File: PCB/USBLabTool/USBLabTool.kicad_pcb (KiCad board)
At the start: 2 copper layers, 9.1 x 5.9 mm, 209 parts, among them J1 Chanel 1 input, J10 T_pwm, J11 T_buf, J12 T_buf, J13 ADC2, J14 ADC1, J15 +3.3VA, J16 +3.3VA, J17 2x01, J18 02x02, J19 T_N5V, J2 Chanel 0 input, J20 USB_C_Receptacle, J3 T_att, J4 T_att, J5 T_acdc, J6 T_acdc, J7 T_amp, J8 T_amp, J9 T_pwm, K1 G5V-2, K2 G5V-2, SW2 PTH_RA_h7.5mm, U1 AQY284SX, U10 Opamp_Quad, U11 DG403, U12 STM32H562VGTx, U13 r1283, U14 XC6206PxxxMR, U15 XC6206PxxxMR, U16 LTC1983ES6-5#TRPBF, U17 TCPP01-M12, U2 AQY284SX, U3 CD74HC4316M96, U4 LMP7718, U5 CD74HC4316M96, U6 LMP7718, U7 OPA863, U8 OPA863, U9 Opamp_Quad, Y1 32.768kHz

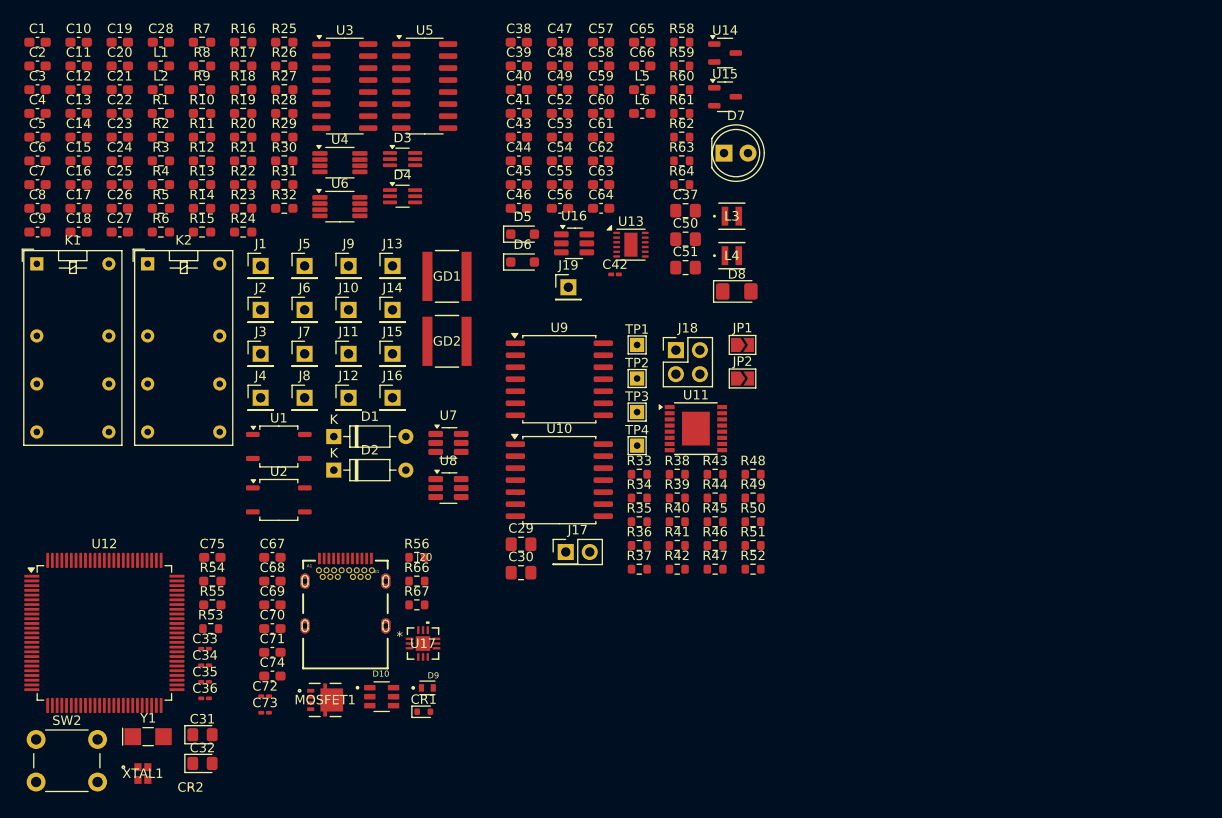
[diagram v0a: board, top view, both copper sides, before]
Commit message: footprint with minor fixes
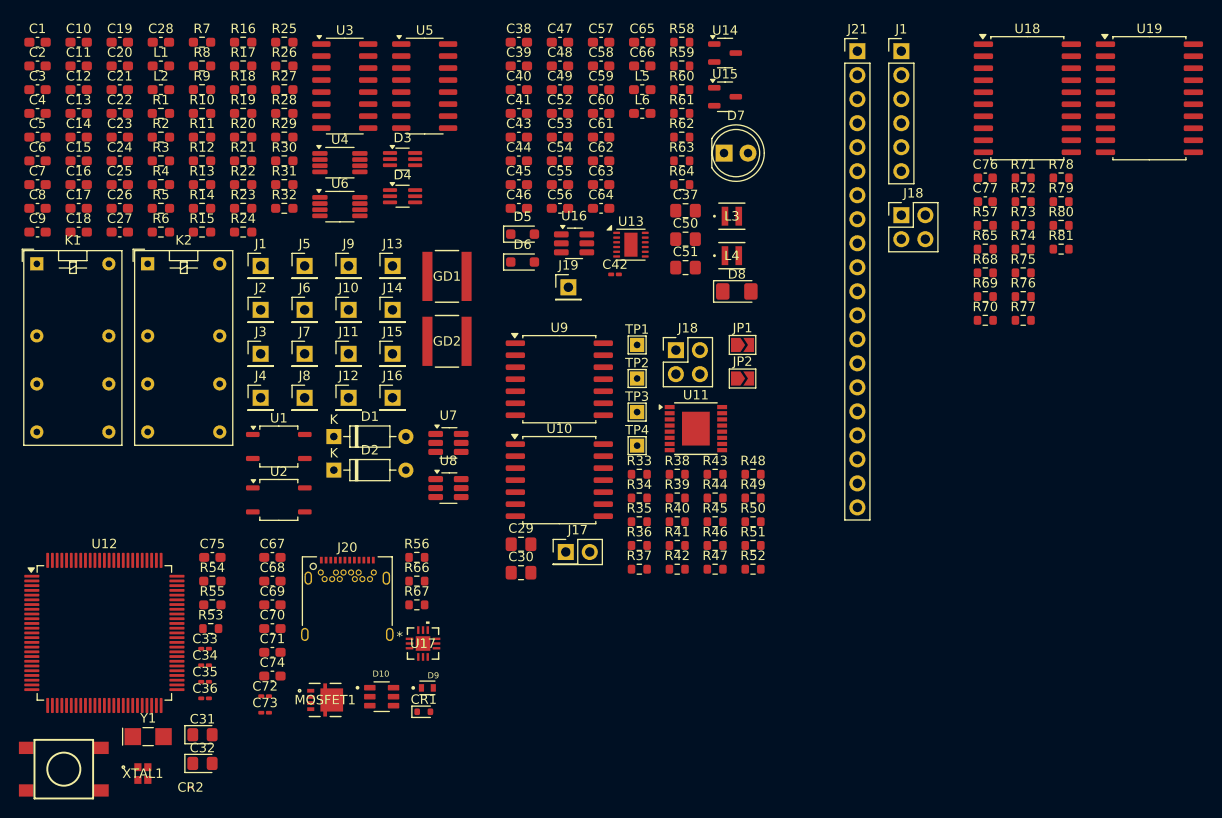
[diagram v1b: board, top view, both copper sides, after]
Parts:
- added C76: 100nF, Capacitor_SMD:C_0603_1608Metric, F.Cu at (206.5, 62.2)
- added C77: 100nF, Capacitor_SMD:C_0603_1608Metric, F.Cu at (206.5, 64.7)
- added J1: Conn_01x06_Pin, Connector_PinHeader_2.54mm:PinHeader_1x06_P2.54mm_Vertical, F.Cu at (197.6, 48.8)
- added J18: 02x02, Connector_PinHeader_2.54mm:PinHeader_2x02_P2.54mm_Vertical, F.Cu at (197.6, 66.2)
- added J21: Conn_01x20_Pin, Connector_PinHeader_2.54mm:PinHeader_1x20_P2.54mm_Vertical, F.Cu at (193.0, 48.8)
- added R57: 1M, Resistor_SMD:R_0603_1608Metric, F.Cu at (206.5, 67.2)
- added R65: 1M, Resistor_SMD:R_0603_1608Metric, F.Cu at (206.5, 69.7)
- added R68: 1M, Resistor_SMD:R_0603_1608Metric, F.Cu at (206.5, 72.3)
- added R69: 1M, Resistor_SMD:R_0603_1608Metric, F.Cu at (206.5, 74.8)
- added R70: 1M, Resistor_SMD:R_0603_1608Metric, F.Cu at (206.5, 77.3)
- added R71: 1M, Resistor_SMD:R_0603_1608Metric, F.Cu at (210.5, 62.2)
- added R72: 1M, Resistor_SMD:R_0603_1608Metric, F.Cu at (210.5, 64.7)
- added R73: 1M, Resistor_SMD:R_0603_1608Metric, F.Cu at (210.5, 67.2)
- added R74: 1M, Resistor_SMD:R_0603_1608Metric, F.Cu at (210.5, 69.7)
- added R75: 1M, Resistor_SMD:R_0603_1608Metric, F.Cu at (210.5, 72.3)
- added R76: 1M, Resistor_SMD:R_0603_1608Metric, F.Cu at (210.5, 74.8)
- added R77: 1M, Resistor_SMD:R_0603_1608Metric, F.Cu at (210.5, 77.3)
- added R78: 1M, Resistor_SMD:R_0603_1608Metric, F.Cu at (214.5, 62.2)
- added R79: 1M, Resistor_SMD:R_0603_1608Metric, F.Cu at (214.5, 64.7)
- added R80: 1M, Resistor_SMD:R_0603_1608Metric, F.Cu at (214.5, 67.2)
- added R81: 1M, Resistor_SMD:R_0603_1608Metric, F.Cu at (214.5, 69.7)
- added U18: 74HC245N, Package_SO:SOIC-20W_7.5x12.8mm_P1.27mm, F.Cu at (210.9, 53.8)
- added U19: 74HC245N, Package_SO:SOIC-20W_7.5x12.8mm_P1.27mm, F.Cu at (223.8, 53.8)
- J20: footprint userfp:CONN RCP USB3.1 TYPEC 24P SMD RA-632723300011 -> Connector_USB:USB_C_Receptacle_Amphenol_12401548E4-2A
- SW2: footprint Button_Switch_THT:SW_PUSH_6mm_H7.3mm -> SparkFun-Switch:Push_SMD_6.2x6.2mm
- moved SW2 4.29 mm to (109.0, 124.8)
- moved J20 0.76 mm to (139.0, 107.7)
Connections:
- GD1 pad 1: Net-(J1-Pin_1) -> P_CH1_IN
- GD2 pad 1: Net-(J2-Pin_1) -> P_CH0_IN
- K1 pad 13: Net-(J1-Pin_1) -> P_CH1_IN
- K2 pad 13: Net-(J2-Pin_1) -> P_CH0_IN
- R56 pad 1: VDD -> +3.3V
- U12 pad 30: unconnected-(U12-PA5-Pad30) -> DAC1_OUT2
- U12 pad 36: CH1_amp_15 -> CH1_amp_5
- U12 pad 37: CH1_amp_12.5 -> CH1_amp_2.5
- U12 pad 55: unconnected-(U12-PD8-Pad55) -> LOGIC_IN8
- U12 pad 56: unconnected-(U12-PD9-Pad56) -> LOGIC_IN9
- U12 pad 57: unconnected-(U12-PD10-Pad57) -> LOGIC_IN10
- U12 pad 58: unconnected-(U12-PD11-Pad58) -> LOGIC_IN11
- U12 pad 59: unconnected-(U12-PD12-Pad59) -> LOGIC_IN12
- U12 pad 60: unconnected-(U12-PD13-Pad60) -> LOGIC_IN13
- U12 pad 61: unconnected-(U12-PD14-Pad61) -> LOGIC_IN14
- U12 pad 62: unconnected-(U12-PD15-Pad62) -> LOGIC_IN15
- U12 pad 81: unconnected-(U12-PD0-Pad81) -> LOGIC_IN0
- U12 pad 82: unconnected-(U12-PD1-Pad82) -> LOGIC_IN1
- U12 pad 83: unconnected-(U12-PD2-Pad83) -> LOGIC_IN2
- U12 pad 84: unconnected-(U12-PD3-Pad84) -> LOGIC_IN3
- U12 pad 85: unconnected-(U12-PD4-Pad85) -> LOGIC_IN4
- U12 pad 86: unconnected-(U12-PD5-Pad86) -> LOGIC_IN5
- U12 pad 87: unconnected-(U12-PD6-Pad87) -> LOGIC_IN6
- U12 pad 88: unconnected-(U12-PD7-Pad88) -> LOGIC_IN7
- U17 pad 12: VDD -> +3.3V
- U5 pad 15: CH0_amp_-1 -> CH0_amp_1
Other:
- board outline removed

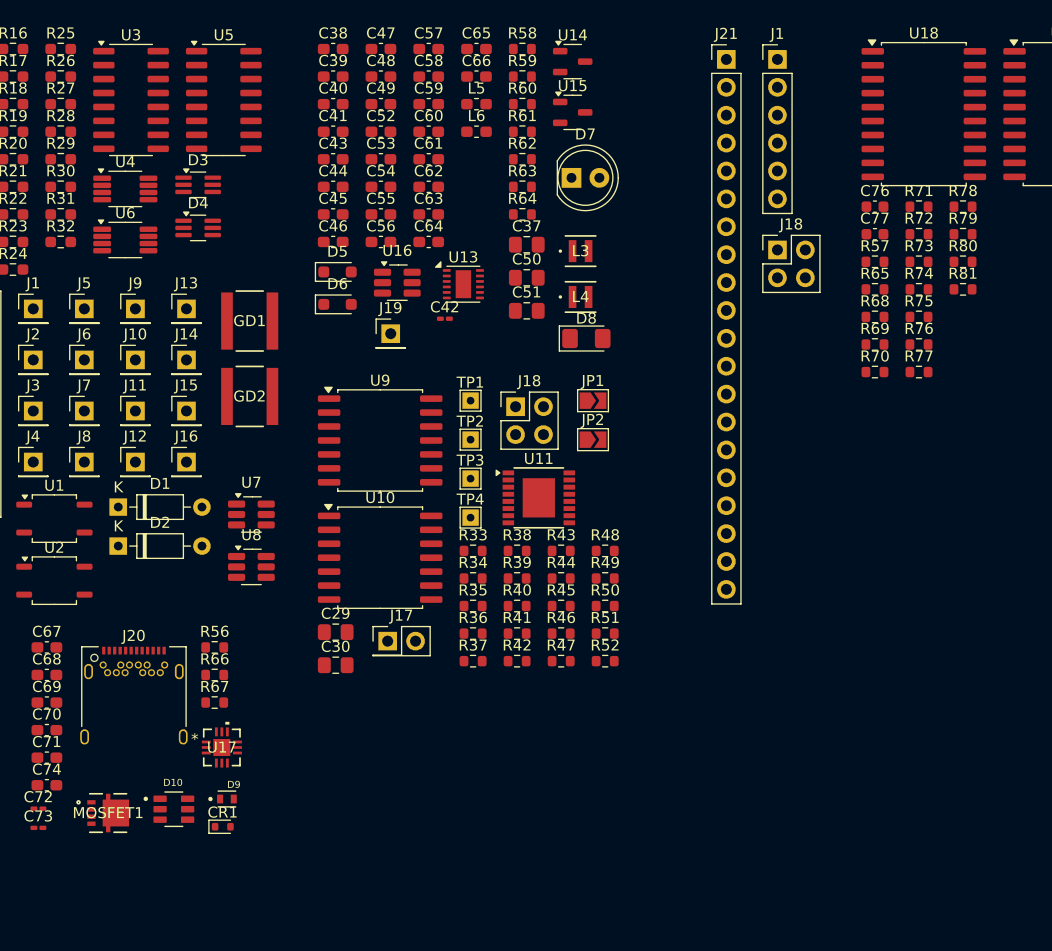
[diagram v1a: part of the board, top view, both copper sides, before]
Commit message: rearrange logic pins, connectors, fix some name tags
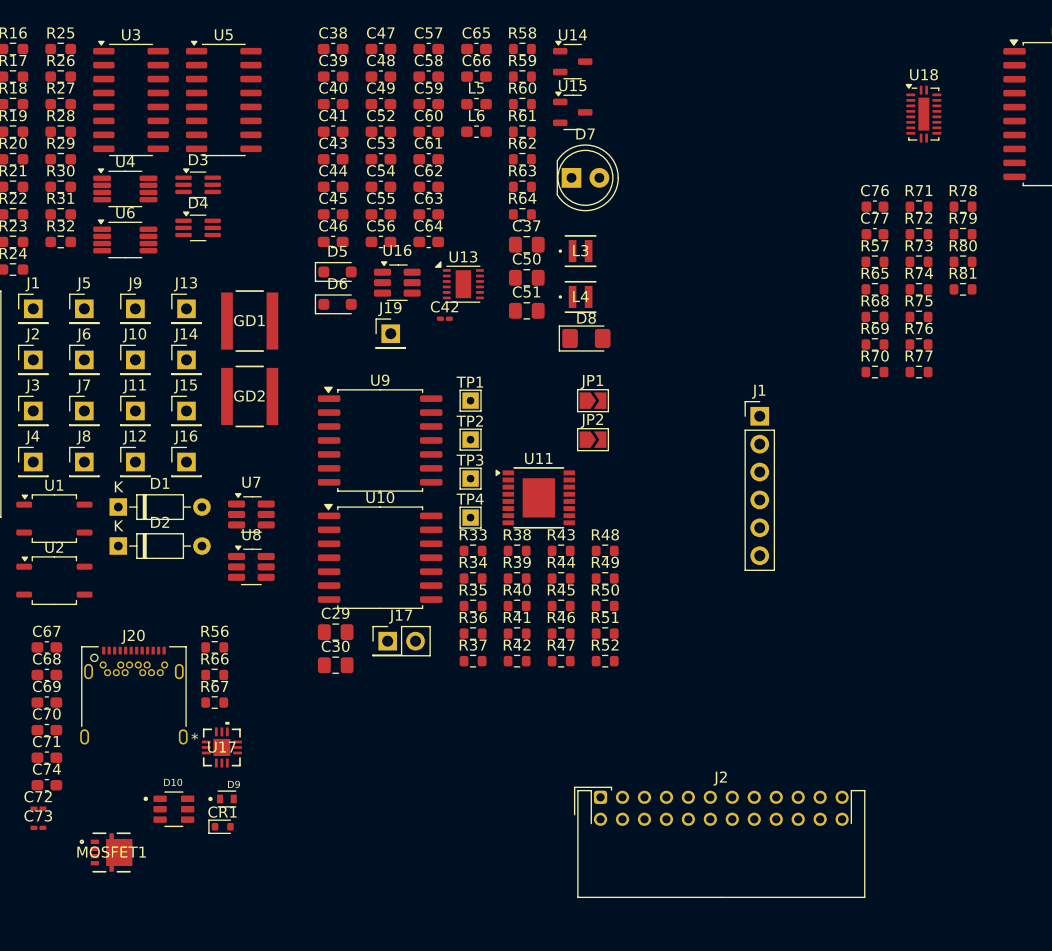
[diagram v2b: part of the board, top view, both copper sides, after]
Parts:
- removed J18 (x2): 02x02, Connector_PinHeader_2.54mm:PinHeader_2x02_P2.54mm_Vertical
- removed J21: Conn_01x20_Pin, Connector_PinHeader_2.54mm:PinHeader_1x20_P2.54mm_Vertical
- added J2: Conn_02x12_Odd_Even, Connector_JST:JST_PHD_S24B-PHDSS_2x12_P2.00mm_Horizontal, F.Cu at (181.5, 116.0)
- U18: footprint Package_SO:SOIC-20W_7.5x12.8mm_P1.27mm -> Package_DFN_QFN:DHVQFN-20-1EP_2.5x4.5mm_P0.5mm_EP1x3mm
- moved J1 32.5 mm to (196.0, 81.3)
- moved MOSFET1 3.61 mm to (137.0, 121.0)
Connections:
- net ADC2_INP7 renamed ADC2_INP3
- C26 pad 1: ADC1 -> ADC1_INP0
- D4 pad 3: ADC1 -> ADC1_INP0
- J14 pad 1: ADC1 -> ADC1_INP0
- R32 pad 2: ADC1 -> ADC1_INP0
- R65 pad 2: LOGIC_INP7 -> LOGIC_INP12
- R68 pad 1: LOGIC_INP12 -> LOGIC_INP9
- R69 pad 2: LOGIC_INP9 -> LOGIC_INP13
- R70 pad 1: LOGIC_INP6 -> LOGIC_INP10
- R71 pad 2: LOGIC_INP11 -> LOGIC_INP14
- R72 pad 1: LOGIC_INP1 -> LOGIC_INP11
- R73 pad 2: LOGIC_INP2 -> LOGIC_INP15
- R74 pad 1: LOGIC_INP10 -> LOGIC_INP0
- R75 pad 2: LOGIC_INP15 -> LOGIC_INP4
- R76 pad 1: LOGIC_INP4 -> LOGIC_INP1
- R77 pad 2: LOGIC_INP14 -> LOGIC_INP5
- R78 pad 1: LOGIC_INP5 -> LOGIC_INP2
- R79 pad 2: LOGIC_INP13 -> LOGIC_INP6
- R80 pad 1: LOGIC_INP0 -> LOGIC_INP3
- R81 pad 2: LOGIC_INP3 -> LOGIC_INP7
- U12 pad 18: CH0 ACDC -> CH0_ACDC
- U12 pad 33: CH1 ACDC -> CH1_ACDC
- U18 pad 11: LOGIC_INP7 -> LOGIC_INP15
- U18 pad 12: LOGIC_INP8 -> LOGIC_INP14
- U18 pad 13: LOGIC_INP9 -> LOGIC_INP13
- U18 pad 16: LOGIC_INP6 -> LOGIC_INP10
- U18 pad 17: LOGIC_INP2 -> LOGIC_INP9
- U18 pad 18: LOGIC_INP1 -> LOGIC_INP8
- U18 pad 2: LOGIC_IN1 -> LOGIC_IN8
- U18 pad 3: LOGIC_IN2 -> LOGIC_IN9
- U18 pad 4: LOGIC_IN6 -> LOGIC_IN10
- U18 pad 7: LOGIC_IN9 -> LOGIC_IN13
- U18 pad 8: LOGIC_IN8 -> LOGIC_IN14
- U18 pad 9: LOGIC_IN7 -> LOGIC_IN15
- U19 pad 11: LOGIC_INP15 -> LOGIC_INP7
- U19 pad 12: LOGIC_INP10 -> LOGIC_INP6
- U19 pad 13: LOGIC_INP14 -> LOGIC_INP5
- U19 pad 15: LOGIC_INP13 -> LOGIC_INP3
- U19 pad 16: LOGIC_INP5 -> LOGIC_INP2
- U19 pad 17: LOGIC_INP3 -> LOGIC_INP1
- U19 pad 3: LOGIC_IN3 -> LOGIC_IN1
- U19 pad 4: LOGIC_IN5 -> LOGIC_IN2
- U19 pad 5: LOGIC_IN13 -> LOGIC_IN3
- U19 pad 7: LOGIC_IN14 -> LOGIC_IN5
- U19 pad 8: LOGIC_IN10 -> LOGIC_IN6
- U19 pad 9: LOGIC_IN15 -> LOGIC_IN7

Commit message: Updated schematic
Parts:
- removed the J1 at (129.8, 71.5)
- removed the J1 at (196.0, 81.3)
- removed the J2 at (129.8, 76.2)
- removed the J2 at (181.5, 116.0)
- removed SW2: PTH_RA_h7.5mm, SparkFun-Switch:Push_SMD_6.2x6.2mm
- added J1: Conn_01x06_Pin, Connector_PinHeader_2.54mm:PinHeader_1x06_P2.54mm_Vertical, F.Cu at (172.5, 55.0)
- added J2: Conn_02x12_Odd_Even, Connector_JST:JST_PHD_S24B-PHDSS_2x12_P2.00mm_Horizontal, F.Cu at (154.7, 42.7)
- added SW1: SW_Push, Button_Switch_THT:SW_PUSH_6mm_H7.3mm, F.Cu at (176.9, 54.7)
- moved C31 77.4 mm to (181.6, 69.8)
- moved C32 77.4 mm to (181.6, 72.8)
- moved XTAL1 76.8 mm to (173.0, 72.2)
- moved CR2 76.5 mm to (159.8, 60.0)
- moved C35 75.5 mm to (180.6, 65.6)
- moved C36 75.5 mm to (180.6, 67.4)
- moved C33 75.5 mm to (180.6, 62.1)
- moved C34 75.5 mm to (180.6, 63.9)
- moved Y1 72.3 mm to (151.3, 57.2)
- moved C38 72.1 mm to (100.1, 91.9)
- moved C39 72.1 mm to (100.1, 94.4)
- moved C40 72.1 mm to (100.1, 97.0)
- moved C43 72.1 mm to (100.1, 102.0)
- moved C44 72.1 mm to (100.1, 104.5)
- moved C47 72.1 mm to (104.5, 91.9)
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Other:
- board outline added: 92.6 x 94.5 mm

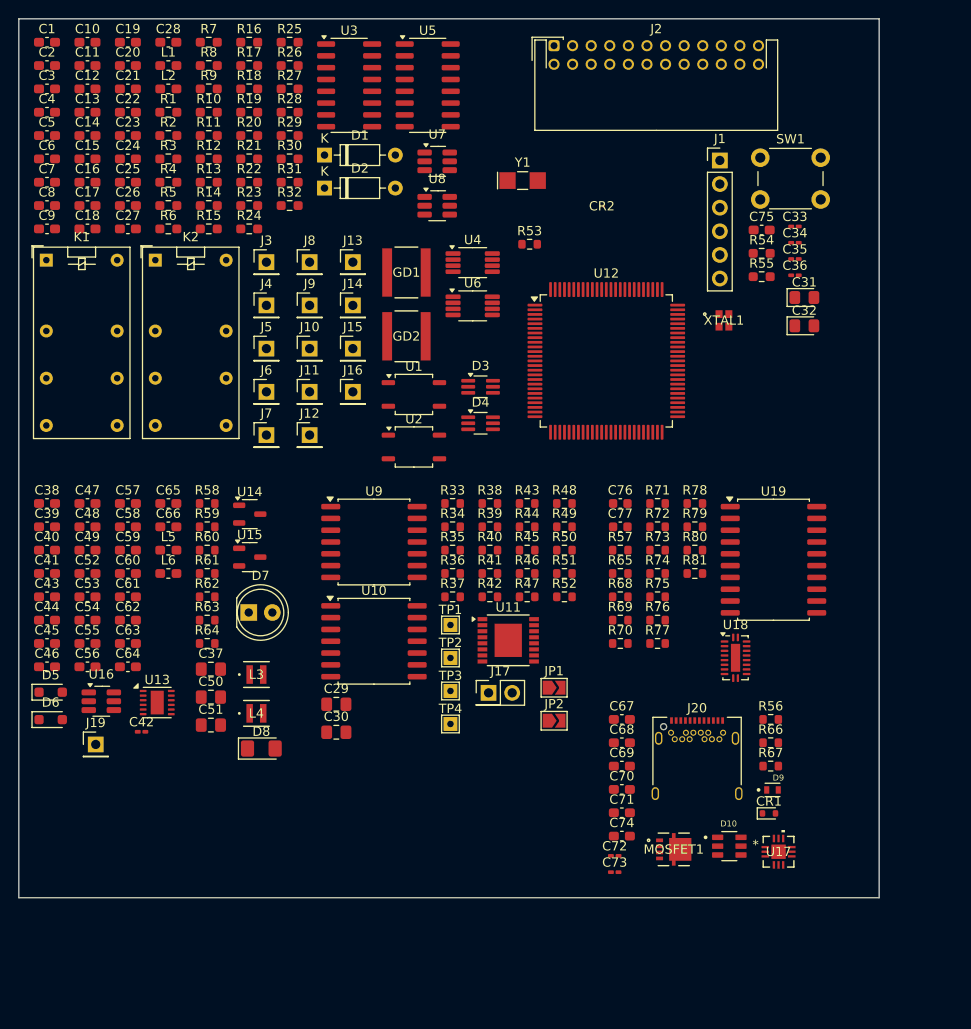
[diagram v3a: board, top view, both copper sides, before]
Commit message: Update logic analyzer schematic
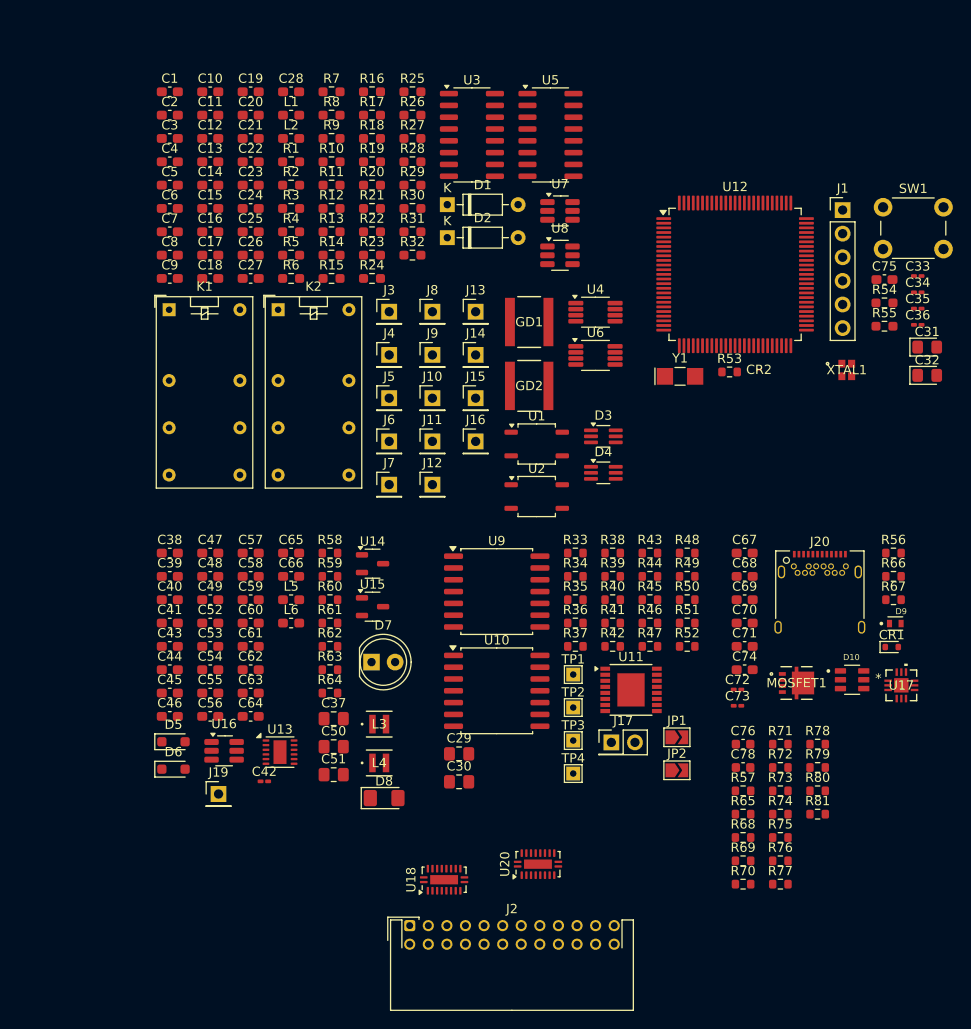
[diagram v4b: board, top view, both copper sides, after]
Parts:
- removed C77: 100nF, Capacitor_SMD:C_0603_1608Metric
- removed U19: 74HC245N, Package_SO:SOIC-20W_7.5x12.8mm_P1.27mm
- added C78: 100nF, Capacitor_SMD:C_0603_1608Metric, F.Cu at (175.0, 120.3)
- added U20: 74HC245, Package_DFN_QFN:DHVQFN-20-1EP_2.5x4.5mm_P0.5mm_EP1x3mm, F.Cu at (152.9, 130.7)
- U18: value 74HC245N -> 74HC245
- moved J2 95.9 mm to (139.2, 137.3)
- moved U18 39.4 mm to (142.8, 132.4), turned to 90 degrees
- moved R65 29.1 mm to (175.0, 125.4)
- moved R68 29.1 mm to (175.0, 127.9)
- moved R72 29.1 mm to (179.0, 120.3)
- moved R74 29.1 mm to (179.0, 125.4)
- moved R75 29.1 mm to (179.0, 127.9)
- moved R79 29.1 mm to (183.0, 120.3)
- moved R81 29.1 mm to (183.0, 125.4)
- moved C76 29.1 mm to (175.0, 117.8)
- moved R57 29.1 mm to (175.0, 122.8)
- moved R69 29.1 mm to (175.0, 130.4)
- moved R70 29.1 mm to (175.0, 132.9)
- moved R71 29.1 mm to (179.0, 117.8)
- moved R73 29.1 mm to (179.0, 122.8)
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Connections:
- R74 pad 1: LOGIC_INP0 -> GND
- R74 pad 2: GND -> LOGIC_INP7
- R75 pad 1: GND -> LOGIC_INP3
- R75 pad 2: LOGIC_INP4 -> GND
- R76 pad 1: LOGIC_INP1 -> GND
- R76 pad 2: GND -> LOGIC_INP6
- R77 pad 1: GND -> LOGIC_INP2
- R77 pad 2: LOGIC_INP5 -> GND
- R78 pad 1: LOGIC_INP2 -> GND
- R78 pad 2: GND -> LOGIC_INP5
- R79 pad 1: GND -> LOGIC_INP1
- R79 pad 2: LOGIC_INP6 -> GND
- R80 pad 1: LOGIC_INP3 -> GND
- R80 pad 2: GND -> LOGIC_INP4
- R81 pad 1: GND -> LOGIC_INP0
- R81 pad 2: LOGIC_INP7 -> GND
- U18 pad 11: LOGIC_INP15 -> LOGIC_IN15
- U18 pad 12: LOGIC_INP14 -> LOGIC_IN14
- U18 pad 13: LOGIC_INP13 -> LOGIC_IN13
- U18 pad 14: LOGIC_INP12 -> LOGIC_IN12
- U18 pad 15: LOGIC_INP11 -> LOGIC_IN11
- U18 pad 16: LOGIC_INP10 -> LOGIC_IN10
- U18 pad 17: LOGIC_INP9 -> LOGIC_IN9
- U18 pad 18: LOGIC_INP8 -> LOGIC_IN8
- U18 pad 2: LOGIC_IN8 -> LOGIC_INP8
- U18 pad 3: LOGIC_IN9 -> LOGIC_INP9
- U18 pad 4: LOGIC_IN10 -> LOGIC_INP10
- U18 pad 5: LOGIC_IN11 -> LOGIC_INP11
- U18 pad 6: LOGIC_IN12 -> LOGIC_INP12
- U18 pad 7: LOGIC_IN13 -> LOGIC_INP13
- U18 pad 8: LOGIC_IN14 -> LOGIC_INP14
- U18 pad 9: LOGIC_IN15 -> LOGIC_INP15
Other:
- board outline removed
